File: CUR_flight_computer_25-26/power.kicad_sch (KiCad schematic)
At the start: 22 parts, among them J2 Screw_Terminal_01x02, J3 Screw_Terminal_01x02, J4 XT30U-M, J5 XT30U-M, U15 ZXCT180B4W5, U16 ZXCT180B4W5, U6 BU33SD5, U7 LM66200

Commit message: Layout power and pyro
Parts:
- removed TP38, TP39: TestPoint, TestPoint_KOASpeer:TestPoint_Chip_RCUCTE_0603, symbol Connector:TestPoint
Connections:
- net BATT_MEAS: now also J2.1 (Pin_1); no longer J2.2 (Pin_2)
- net BATT_SWITCH: now also J2.2 (Pin_2); no longer J2.1 (Pin_1)
- net PYRO_BATT_MEAS: now also J3.2 (Pin_2); no longer J3.1 (Pin_1)
- net PYRO_BATT_SWITCH: now also J3.1 (Pin_1); no longer J3.2 (Pin_2)

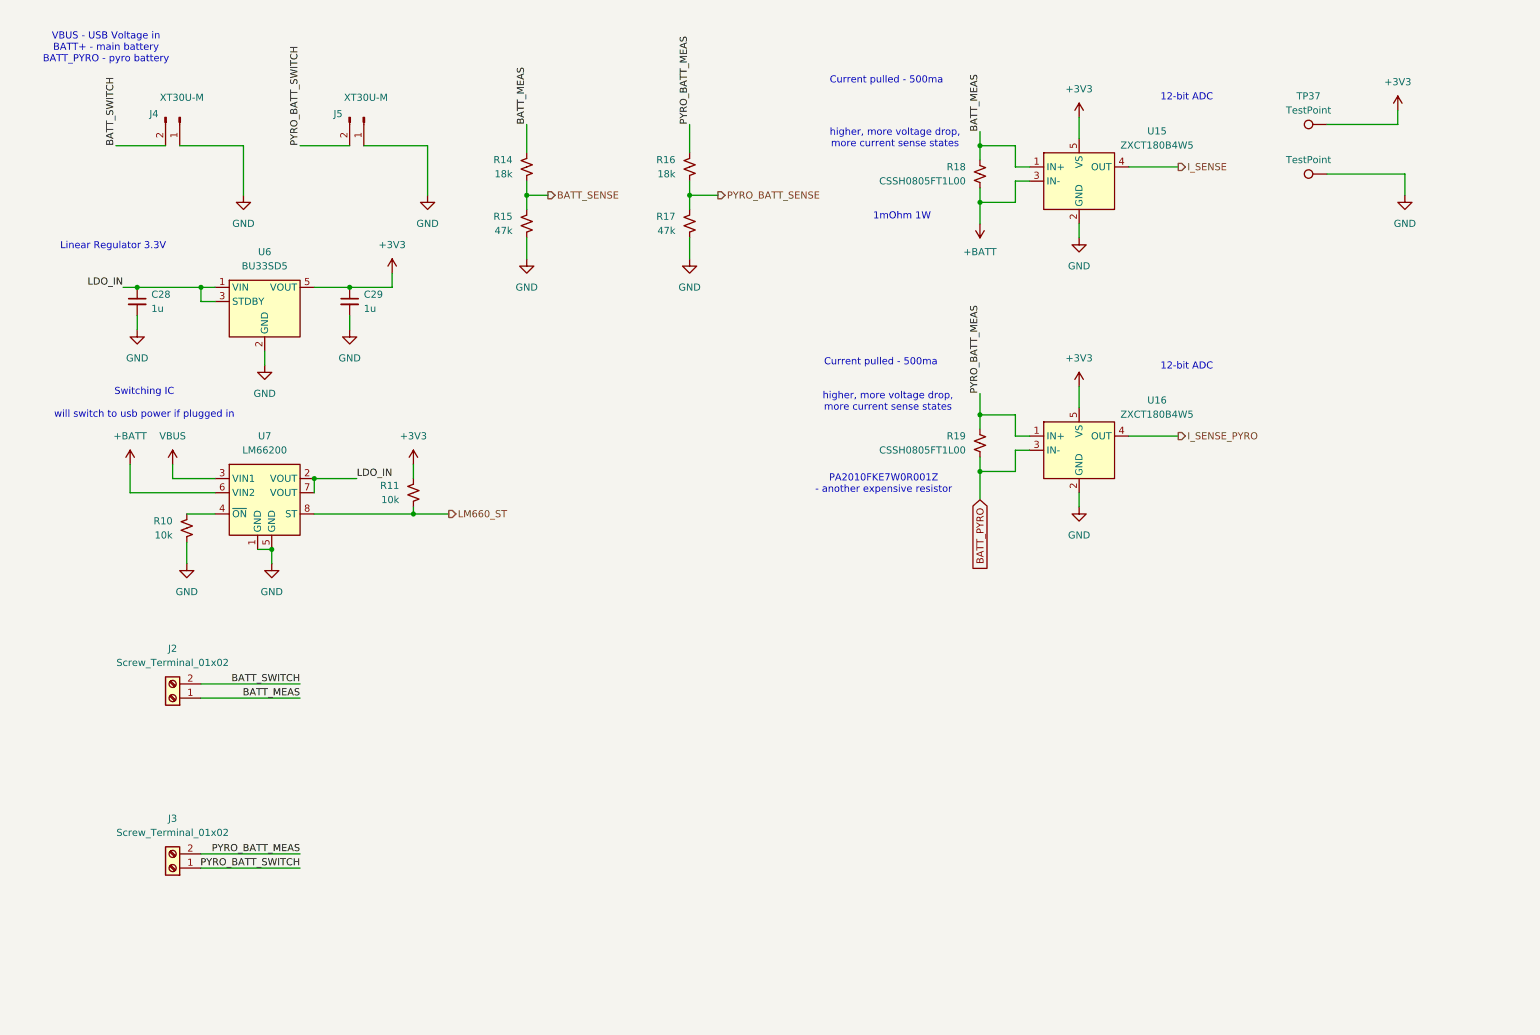
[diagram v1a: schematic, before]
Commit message: Replace LDO
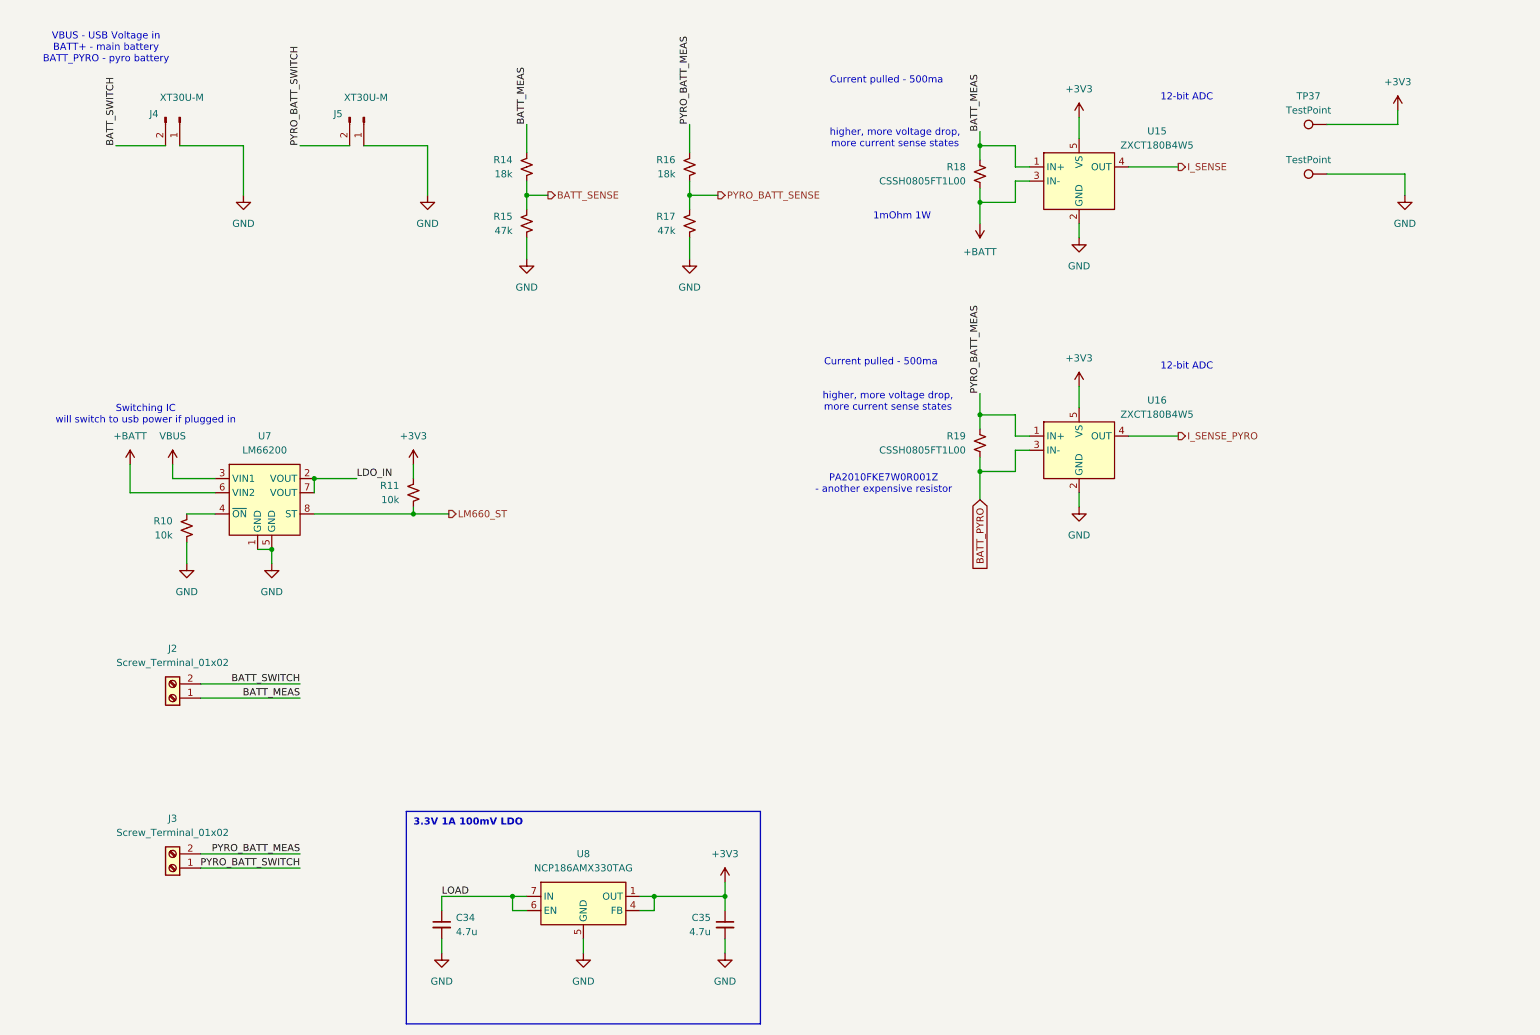
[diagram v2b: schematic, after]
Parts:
- removed C28, C29: 1u, Capacitor_SMD:C_0603_1608Metric, symbol Device:C_Small
- removed U6: BU33SD5, BUxxSD5:SSOP5_ROM, symbol BUxxSD5:BU33SD5
- added C34, C35: 4.7u, symbol Device:C_Small
- added U8: NCP186AMX330TAG, Package_DFN_QFN:DFN-6-1EP_1.2x1.2mm_P0.4mm_EP0.3x0.94mm_PullBack, symbol Regulator_Linear_onsemi:NCP186AMX330TAG
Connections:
- net +3V3: now also C35.1, U8.1 (OUT), U8.2 (OUT), U8.4 (FB)
- net GND: now also C34.2, C35.2, U8.3 (N/C), U8.5 (GND), U8.9 (EPAD)
- new net IN: C34.1, U8.6 (EN), U8.7 (IN), U8.8 (IN)
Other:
- note added: "3.3V 1A 100mV LDO"
- note removed: "Linear Regulator 3.3V"

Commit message: updated pcb for ddrc
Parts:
- C34, C35: value 4.7u -> 1u; footprint (none) -> Capacitor_SMD:C_0603_1608Metric
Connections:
- net LDO_IN is gone; now on net IN: U7.2 (VOUT), U7.7 (VOUT)
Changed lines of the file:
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@@
 		)
 	)
-	(label "LOAD"
+	(label "LDO_IN"
 		(at 88.9 171.45 0)
 		(effects
@@
 			)
 		)
-		(property "Value" "4.7u"
+		(property "Value" "1u"
 			(at 137.16 177.8062 0)
 			(effects
@@
 			)
 		)
-		(property "Footprint" ""
+		(property "Footprint" "Capacitor_SMD:C_0603_1608Metric"
 			(at 139.7 176.53 0)
 			(effects
@@
 			)
 		)
-		(property "Value" "4.7u"
+		(property "Value" "1u"
 			(at 91.44 177.8062 0)
 			(effects
@@
 			)
 		)
-		(property "Footprint" ""
+		(property "Footprint" "Capacitor_SMD:C_0603_1608Metric"
 			(at 88.9 176.53 0)
 			(effects

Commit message: Fix LDO footprint
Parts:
- U8: footprint Package_DFN_QFN:DFN-6-1EP_1.2x1.2mm_P0.4mm_EP0.3x0.94mm_PullBack -> XDFN8_1P6X1P2_onsemi:XDFN8_1P6X1P2_onsemi
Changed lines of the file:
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@@
 			)
 		)
-		(property "Footprint" "Package_DFN_QFN:DFN-6-1EP_1.2x1.2mm_P0.4mm_EP0.3x0.94mm_PullBack"
+		(property "Footprint" "XDFN8_1P6X1P2_onsemi:XDFN8_1P6X1P2_onsemi"
 			(at 114.3 168.91 0)
 			(effects

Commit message: Apply MPNs for capacitors and connectors
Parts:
- C34, C35: MPN (none) -> C0603C105K4RACTU
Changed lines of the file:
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@@
+			)
+		)
+		(property "MPN" "C0603C105K4RACTU"
+			(at 139.7 176.53 0)
+			(effects
+				(font
+					(size 1.27 1.27)
+				)
 			)
 		)
@@
 			)
 		)
+		(property "MPN" "C0603C105K4RACTU"
+			(at 88.9 176.53 0)
+			(effects
+				(font
+					(size 1.27 1.27)
+				)
+			)
+		)

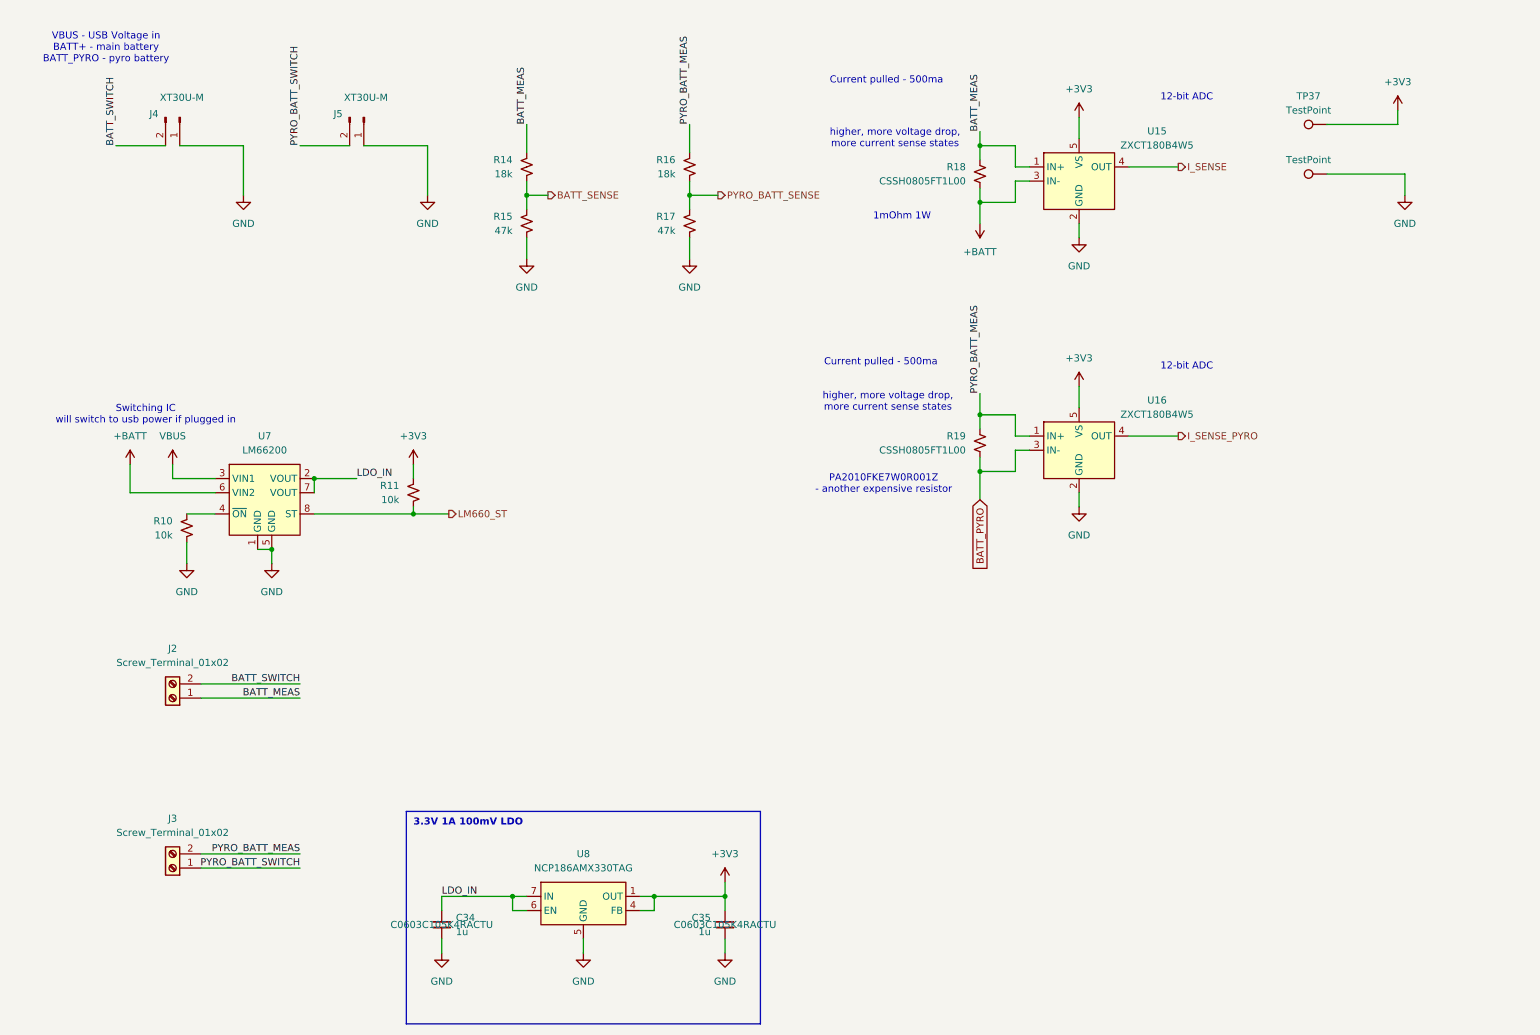
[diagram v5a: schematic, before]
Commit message: Add MPNs for ICs
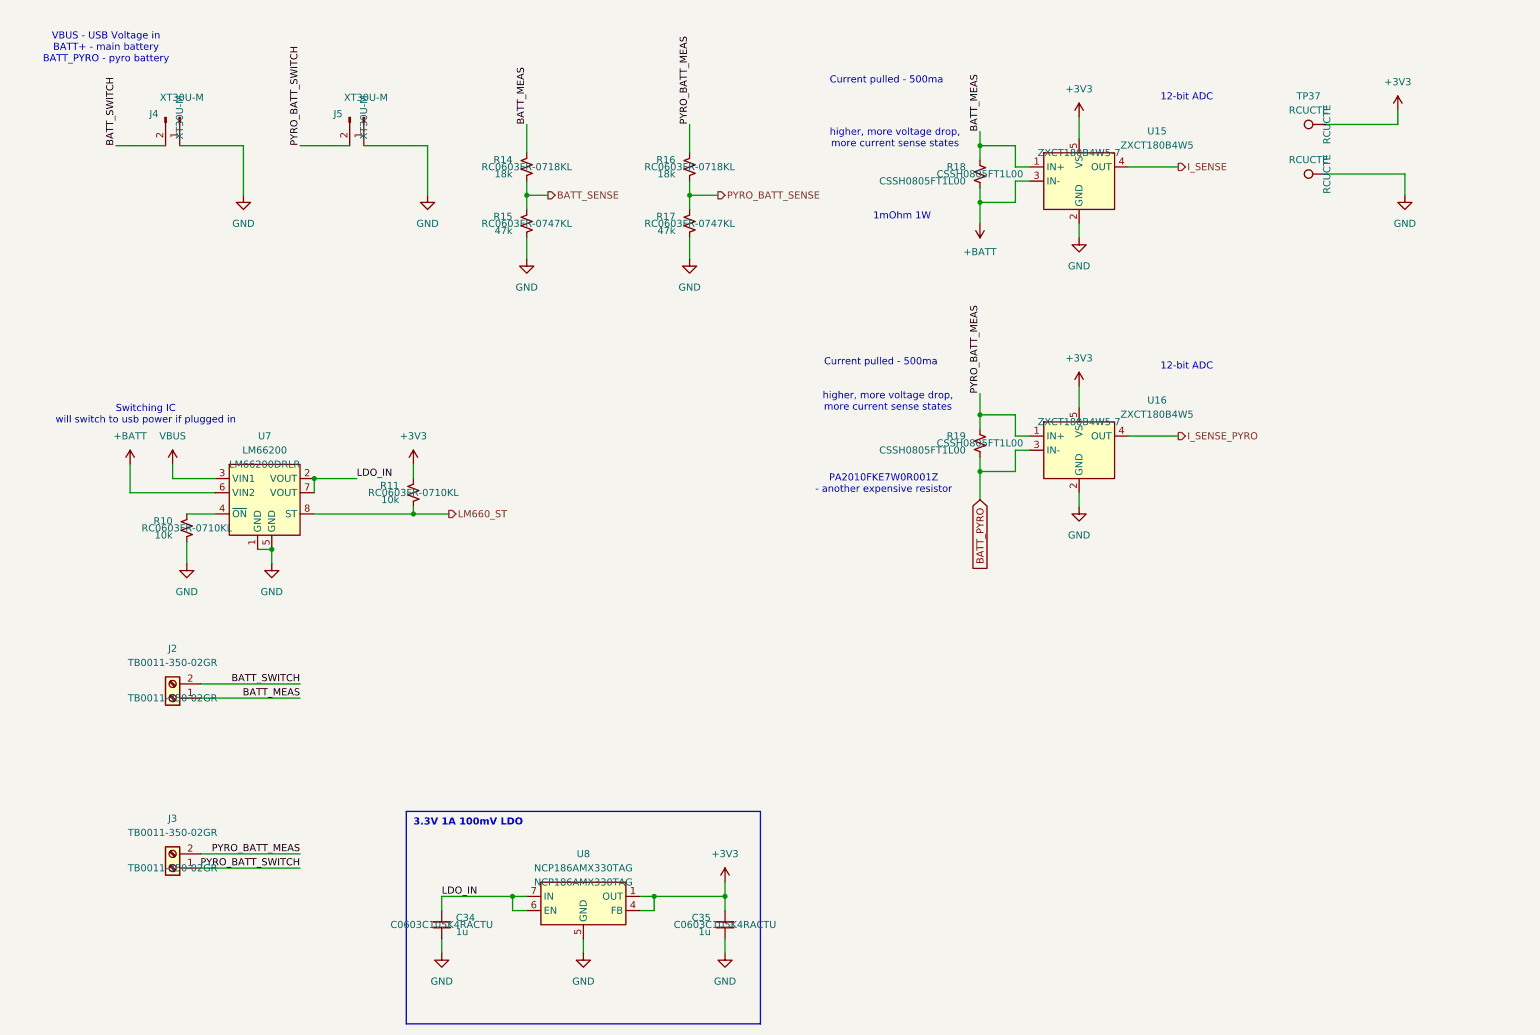
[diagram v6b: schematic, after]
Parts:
- J2, J3: value Screw_Terminal_01x02 -> TB0011-350-02GR; MPN (none) -> TB0011-350-02GR
- J4, J5: MPN (none) -> XT30U-M
- R10, R11: MPN (none) -> RC0603FR-0710KL
- R14, R16: MPN (none) -> RC0603FR-0718KL
- R15, R17: MPN (none) -> RC0603FR-0747KL
- R18, R19: MPN (none) -> CSSH0805FT1L00
- TP37, TP40: value TestPoint -> RCUCTE; MPN (none) -> RCUCTE
- U15, U16: MPN (none) -> ZXCT180B4W5-7
- U7: MPN (none) -> LM66200DRLR
- U8: MPN (none) -> NCP186AMX330TAG
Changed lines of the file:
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@@
+			)
+		)
+		(property "MPN" "RC0603FR-0718KL"
+			(at 133.35 40.64 0)
+			(effects
+				(font
+					(size 1.27 1.27)
+				)
 			)
 		)
@@
 			)
 		)
+		(property "MPN" "NCP186AMX330TAG"
+			(at 114.3 168.91 0)
+			(effects
+				(font
+					(size 1.27 1.27)
+				)
+			)
+		)
 		(pin "7"
 		)
@@
 			)
 		)
-		(property "Value" "Screw_Terminal_01x02"
+		(property "Value" "TB0011-350-02GR"
 			(at 40.64 129.54 0)
 			(effects
@@
 			)
 		)
+		(property "MPN" "TB0011-350-02GR"
+			(at 40.64 135.89 0)
+			(effects
+				(font
+					(size 1.27 1.27)
+				)
+			)
+		)
 		(pin "2"
 		)
@@
 			)
 		)
-		(property "Value" "TestPoint"
+		(property "Value" "RCUCTE"
 			(at 244.348 39.37 90)
 			(effects
@@
 			)
 		)
+		(property "MPN" "RCUCTE"
+			(at 247.65 41.91 0)
+			(effects
+				(font
+					(size 1.27 1.27)
+				)
+			)
+		)
 		(pin "1"
 		)
@@
 			)
 		)
+		(property "MPN" "CSSH0805FT1L00"
+			(at 185.42 90.17 0)
+			(effects
+				(font
+					(size 1.27 1.27)
+				)
+			)
+		)
 		(pin "2"
 		)
@@
 			)
 		)
-		(property "Value" "TestPoint"
+		(property "Value" "RCUCTE"
 			(at 244.348 30.48 90)
 			(effects
@@
 			)
 		)
+		(property "MPN" "RCUCTE"
+			(at 247.65 33.02 0)
+			(effects
+				(font
+					(size 1.27 1.27)
+				)
+			)
+		)
 		(pin "1"
 		)
@@
 			)
 		)
-		(property "Value" "Screw_Terminal_01x02"
+		(property "Value" "TB0011-350-02GR"
 			(at 40.64 160.02 0)
 			(effects
@@
 				)
 				(hide yes)
+			)
+		)
+		(property "MPN" "TB0011-350-02GR"
+			(at 40.64 166.37 0)
+			(effects
+				(font
+					(size 1.27 1.27)
+				)
 			)
 		)
@@
 			)
 		)
+		(property "MPN" "XT30U-M"
+			(at 74.93 31.75 0)
+			(effects
+				(font
+					(size 1.27 1.27)
+				)
+			)
+		)
 		(pin "1"
 		)
@@
 				)
 				(hide yes)
+			)
+		)
+		(property "MPN" "ZXCT180B4W5-7"
+			(at 203.2 86.36 0)
+			(effects
+				(font
+					(size 1.27 1.27)
+				)
 			)
 		)
@@
 			)
 		)
+		(property "MPN" "RC0603FR-0747KL"
+			(at 104.14 50.8 0)
+			(effects
+				(font
+					(size 1.27 1.27)
+				)
+			)
+		)
 		(pin "1"
 		)
@@
 				)
 				(hide yes)
+			)
+		)
+		(property "MPN" "LM66200DRLR"
+			(at 57.15 93.98 0)
+			(effects
+				(font
+					(size 1.27 1.27)
+				)
 			)
 		)
@@
 			)
 		)
+		(property "MPN" "RC0603FR-0718KL"
+			(at 104.14 40.64 0)
+			(effects
+				(font
+					(size 1.27 1.27)
+				)
+			)
+		)
 		(pin "1"
 		)
@@
 			)
 		)
+		(property "MPN" "RC0603FR-0710KL"
+			(at 83.82 99.06 0)
+			(effects
+				(font
+					(size 1.27 1.27)
+				)
+			)
+		)
 		(pin "1"
 		)
@@
 			)
 		)
+		(property "MPN" "RC0603FR-0710KL"
+			(at 43.18 105.41 0)
+			(effects
+				(font
+					(size 1.27 1.27)
+				)
+			)
+		)
 		(pin "1"
 		)
@@
 				)
 				(hide yes)
+			)
+		)
+		(property "MPN" "CSSH0805FT1L00"
+			(at 185.42 41.91 0)
+			(effects
+				(font
+					(size 1.27 1.27)
+				)
 			)
 		)
@@
 			)
 		)
+		(property "MPN" "RC0603FR-0747KL"
+			(at 133.35 50.8 0)
+			(effects
+				(font
+					(size 1.27 1.27)
+				)
+			)
+		)
 		(pin "1"
 		)
@@
 				)
 				(hide yes)
+			)
+		)
+		(property "MPN" "ZXCT180B4W5-7"
+			(at 203.2 38.1 0)
+			(effects
+				(font
+					(size 1.27 1.27)
+				)
 			)
 		)
@@
 			)
 		)
+		(property "MPN" "XT30U-M"
+			(at 41.91 31.75 0)
+			(effects
+				(font
+					(size 1.27 1.27)
+				)
+			)
+		)
